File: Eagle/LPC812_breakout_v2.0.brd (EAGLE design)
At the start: 30.5 x 15.2 mm, 11 parts

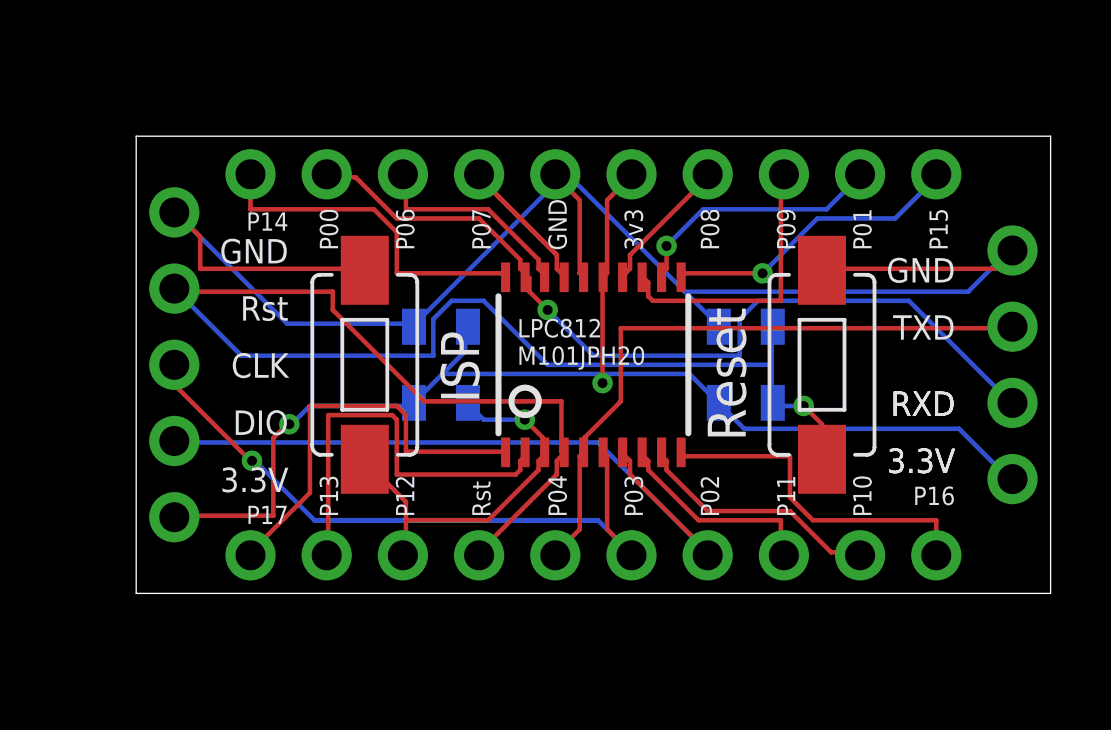
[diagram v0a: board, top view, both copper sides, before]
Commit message: Revision 2
Changes:

- 10 mil traces, no 90° bends, ground plane where possible.
- Font size for pin labelling increased.
- Removed SWD port to reduce complexity and size. If needed, the board
can be accessed at the broken out pins.
- Included 3.3V regulator, since the driving ability of those includede
in the USB to serial converters is limited.
- Removed debouncing cap from reset switch.
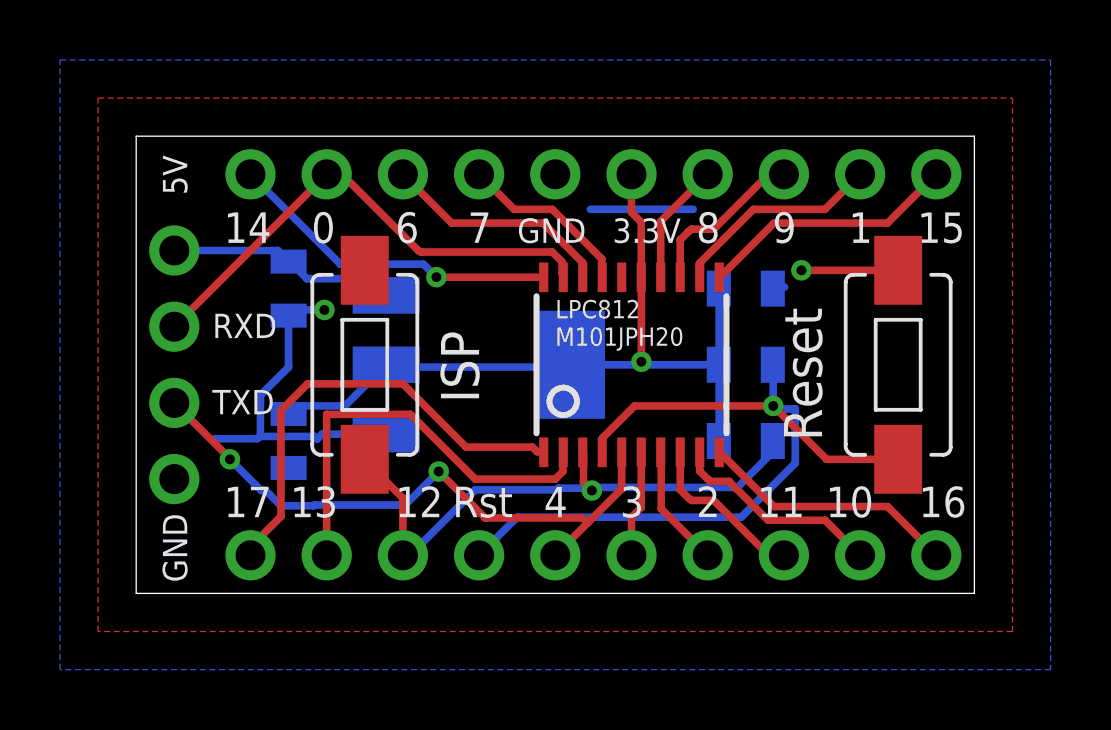
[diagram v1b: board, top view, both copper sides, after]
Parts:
- removed JP5: (no value), microbuilder:1X05_ROUND
- added C2: 10u, SparkFun-Capacitors:0805
- added IC1: (no value), SparkFun-PowerIC:SOT223
- added U$2: (no value), SparkFun-Aesthetics:OSHW-LOGO-S
- C3: value 100n -> 10u
- moved JP3 27.9 mm to (1.27, 7.62), turned to 270 degrees
- moved R1 10.2 mm to (20.3, 5.08)
- moved C3 5.24 mm to (5.08, 10.2), turned to 270 degrees
- moved S2 2.54 mm to (25.4, 7.62)
- moved U$1 1.27 mm to (16.5, 7.62)
- moved R2 1.27 mm to (20.3, 7.62)
- moved C1 1.27 mm to (20.3, 10.2), turned to 180 degrees
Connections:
- new net 5V: C3.1, IC1.3, JP3.1
- net 3.3V: now also C1.1, C2.1, IC1.2, IC1.4; no longer C3.1, JP3.1, JP5.1
- net GND: now also C2.2, IC1.1; no longer JP5.5
- net NRES: no longer C1.1, JP5.4
- net P6: no longer JP5.3
- net P7: no longer JP5.2
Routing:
- net GND: track 54.3 -> 18.7 mm, vias 0 -> 2
- net P6: track 31.6 -> 3.57 mm, vias 1 -> 0
- net NRES: track 50.0 -> 27.3 mm
- net P7: track 24.0 -> 4.09 mm
- net 3.3V: track 42.5 -> 26.7 mm, vias 2 -> 1
- net P19: track 28.8 -> 16.8 mm, vias 1 -> 0
- net 5V: track 0.00 -> 7.68 mm
- net P3: track 13.1 -> 19.5 mm
- net P13: track 9.47 -> 5.60 mm
- net P10: track 11.4 -> 8.66 mm
- net P17: track 8.26 -> 5.88 mm
- net P1: track 13.7 -> 15.3 mm
- net P12: track 8.57 -> 7.05 mm, vias 1 -> 0
- net P8: track 6.98 -> 5.60 mm
- net P11: track 9.99 -> 8.66 mm, vias 1 -> 0
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- added copper zone on layer 1, net GND
- added copper zone on layer 16, net GND
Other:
- board size 30.5 x 15.2 mm -> 27.9 x 15.2 mm
- board text added: "0"
- board text added: "1"
- board text added: "10"
- board text added: "11"
- board text added: "12"
- board text added: "13"
- board text added: "14"
- board text added: "15"
- board text added: "16"
- board text added: "17"
- board text added: "2"
- board text added: "3"
- board text added: "4"
- board text added: "5V"
- board text added: "6"
- board text added: "7"
- board text added: "8"
- board text added: "9"
- board text added: "BB-LPC812 V2"
- board text added: "C1"
- board text added: "C2"
- board text added: "C3"
- board text added: "R1"
- board text added: "R2"
- board text added: "cpldcpu 9/13"
- board text removed: "3v3"
- board text removed: "CLK"
- board text removed: "DIO"
- board text removed: "LPC812 Breakout cpldcpu 9/2013"
- board text removed: "P00"
- board text removed: "P01"
- board text removed: "P02"
- board text removed: "P03"
- board text removed: "P04"
- board text removed: "P06"
- board text removed: "P07"
- board text removed: "P08"
- board text removed: "P09"
- board text removed: "P10"
- board text removed: "P11"
- board text removed: "P12"
- board text removed: "P13"
- board text removed: "P14"
- board text removed: "P15"
- board text removed: "P16"
- board text removed: "P17"
